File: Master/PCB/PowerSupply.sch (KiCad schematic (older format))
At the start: 32 parts, among them J20 Jumper, Q28 BSS138, Q29 BSS138, Q30 BSS138, U19 LM5165YDRC

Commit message: Update
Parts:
- C89, C90: value 1u -> 10u; footprint Capacitors_SMD:C_0603_HandSoldering -> Capacitor_SMD:C_0805_2012Metric
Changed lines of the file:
@@
 $Descr A2 23386 16535
 encoding utf-8
-Sheet 8 8
+Sheet 7 8
 Title ""
 Date ""
@@
 P 12400 6850
 F 0 "C90" H 12200 6800 50  0000 L CNN
-F 1 "1u" H 12200 6900 50  0000 L CNN
-F 2 "Capacitors_SMD:C_0603_HandSoldering" H 12438 6700 50  0001 C CNN
+F 1 "10u" H 12200 6900 50  0000 L CNN
+F 2 "Capacitor_SMD:C_0805_2012Metric" H 12438 6700 50  0001 C CNN
 F 3 "~" H 12400 6850 50  0001 C CNN
 F 4 "50V" H 12400 6850 50  0001 C CNN "Volatge"
@@
 P 11900 6850
 F 0 "C89" H 11700 6800 50  0000 L CNN
-F 1 "1u" H 11700 6900 50  0000 L CNN
-F 2 "Capacitors_SMD:C_0603_HandSoldering" H 11938 6700 50  0001 C CNN
+F 1 "10u" H 11700 6900 50  0000 L CNN
+F 2 "Capacitor_SMD:C_0805_2012Metric" H 11938 6700 50  0001 C CNN
 F 3 "~" H 11900 6850 50  0001 C CNN
 F 4 "50V" H 11900 6850 50  0001 C CNN "Volatge"

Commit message: Current sensors updates & master
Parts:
- C89, C90: footprint Capacitor_SMD:C_0805_2012Metric -> Capacitors_SMD:C_0805_HandSoldering
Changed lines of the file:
@@
 EESchema Schematic File Version 5
 LIBS:BMS-Master-cache
-EELAYER 29 0
+EELAYER 30 0
 EELAYER END
 $Descr A2 23386 16535
 encoding utf-8
-Sheet 7 8
+Sheet 6 7
 Title ""
 Date ""
@@
 F 0 "C90" H 12200 6800 50  0000 L CNN
 F 1 "10u" H 12200 6900 50  0000 L CNN
-F 2 "Capacitor_SMD:C_0805_2012Metric" H 12438 6700 50  0001 C CNN
+F 2 "Capacitors_SMD:C_0805_HandSoldering" H 12438 6700 50  0001 C CNN
 F 3 "~" H 12400 6850 50  0001 C CNN
 F 4 "50V" H 12400 6850 50  0001 C CNN "Volatge"
@@
 F 0 "C89" H 11700 6800 50  0000 L CNN
 F 1 "10u" H 11700 6900 50  0000 L CNN
-F 2 "Capacitor_SMD:C_0805_2012Metric" H 11938 6700 50  0001 C CNN
+F 2 "Capacitors_SMD:C_0805_HandSoldering" H 11938 6700 50  0001 C CNN
 F 3 "~" H 11900 6850 50  0001 C CNN
 F 4 "50V" H 11900 6850 50  0001 C CNN "Volatge"

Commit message: BOM
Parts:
- C88, C89, C90, C91, C92, C93, C94: symbol BMS-Master-rescue:C-Device -> BMS-Master-rescue:C-Device-BMS-Master-rescue
- J20: symbol BMS-Master-rescue:Conn_01x01-Connector_Generic -> BMS-Master-rescue:Conn_01x01-Connector_Generic-BMS-Master-rescue
- R172, R173, R174, R175, R176, R177, R178, R179, R180, R181, R182, R183: symbol BMS-Master-rescue:R-Device -> BMS-Master-rescue:R-Device-BMS-Master-rescue
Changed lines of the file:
@@
 EESchema Schematic File Version 5
 LIBS:BMS-Master-cache
-EELAYER 30 0
+EELAYER 29 0
 EELAYER END
 $Descr A2 23386 16535
@@
 $EndComp
 $Comp
-L BMS-Master-rescue:C-Device C90
+L BMS-Master-rescue:C-Device-BMS-Master-rescue C90
 U 1 1 5C6103A5
 P 12400 6850
@@
 $EndComp
 $Comp
-L BMS-Master-rescue:C-Device C89
+L BMS-Master-rescue:C-Device-BMS-Master-rescue C89
 U 1 1 5C61074A
 P 11900 6850
@@
 	12400 6700 12400 6400
 $Comp
-L BMS-Master-rescue:GND-power #PWR0251
+L BMS-Master-rescue:GND-power-BMS-Master-rescue #PWR0251
 U 1 1 5C6188F7
 P 11900 7350
@@
 	11900 7000 11900 7350
 $Comp
-L BMS-Master-rescue:GND-power #PWR0252
+L BMS-Master-rescue:GND-power-BMS-Master-rescue #PWR0252
 U 1 1 5C61B805
 P 12400 7350
@@
 Connection ~ 13350 7150
 $Comp
-L BMS-Master-rescue:GND-power #PWR0253
+L BMS-Master-rescue:GND-power-BMS-Master-rescue #PWR0253
 U 1 1 5C69C12E
 P 13900 7600
@@
 	13900 7350 13900 7600
 $Comp
-L BMS-Master-rescue:R-Device R179
+L BMS-Master-rescue:R-Device-BMS-Master-rescue R179
 U 1 1 5C69FE87
 P 14400 7250
@@
 	14400 7000 14500 7000
 $Comp
-L BMS-Master-rescue:R-Device R177
+L BMS-Master-rescue:R-Device-BMS-Master-rescue R177
 U 1 1 5C627140
 P 13750 6800
@@
 $EndComp
 $Comp
-L BMS-Master-rescue:R-Device R175
+L BMS-Master-rescue:R-Device-BMS-Master-rescue R175
 U 1 1 5C623C3B
 P 13350 6800
@@
 $EndComp
 $Comp
-L BMS-Master-rescue:GND-power #PWR0254
+L BMS-Master-rescue:GND-power-BMS-Master-rescue #PWR0254
 U 1 1 5C6A8028
 P 13350 7600
@@
 	13700 8500 14650 8500
 $Comp
-L BMS-Master-rescue:R-Device R178
+L BMS-Master-rescue:R-Device-BMS-Master-rescue R178
 U 1 1 5C6F3B76
 P 14150 9100
@@
 	15850 6600 15850 6400
 $Comp
-L BMS-Master-rescue:GND-power #PWR0255
+L BMS-Master-rescue:GND-power-BMS-Master-rescue #PWR0255
 U 1 1 5C713381
 P 14400 7600
@@
 	13400 10700 13650 10700
 $Comp
-L BMS-Master-rescue:R-Device R176
+L BMS-Master-rescue:R-Device-BMS-Master-rescue R176
 U 1 1 5C72D283
 P 13650 10850
@@
 	13650 10700 13850 10700
 $Comp
-L BMS-Master-rescue:GND-power #PWR0256
+L BMS-Master-rescue:GND-power-BMS-Master-rescue #PWR0256
 U 1 1 5C72DA2B
 P 13650 11100
@@
 Connection ~ 13650 11100
 $Comp
-L BMS-Master-rescue:R-Device R182
+L BMS-Master-rescue:R-Device-BMS-Master-rescue R182
 U 1 1 5C737745
 P 16900 6400
@@
 Connection ~ 15850 6400
 $Comp
-L BMS-Master-rescue:R-Device R180
+L BMS-Master-rescue:R-Device-BMS-Master-rescue R180
 U 1 1 5C7417D6
 P 16250 6850
@@
 $EndComp
 $Comp
-L BMS-Master-rescue:GND-power #PWR0257
+L BMS-Master-rescue:GND-power-BMS-Master-rescue #PWR0257
 U 1 1 5C7421FF
 P 16250 7700
@@
 $EndComp
 $Comp
-L BMS-Master-rescue:C-Device C92
+L BMS-Master-rescue:C-Device-BMS-Master-rescue C92
 U 1 1 5C742B3F
 P 16250 7350
@@
 	16550 7500 16550 7700
 $Comp
-L BMS-Master-rescue:C-Device C93
+L BMS-Master-rescue:C-Device-BMS-Master-rescue C93
 U 1 1 5C742FAA
 P 16550 7350
@@
 $EndComp
 $Comp
-L BMS-Master-rescue:GND-power #PWR0258
+L BMS-Master-rescue:GND-power-BMS-Master-rescue #PWR0258
 U 1 1 5C74287E
 P 16550 7700
@@
 $EndComp
 $Comp
-L BMS-Master-rescue:R-Device R181
+L BMS-Master-rescue:R-Device-BMS-Master-rescue R181
 U 1 1 5C741EBD
 P 16550 6850
@@
 	17450 7500 17450 7700
 $Comp
-L BMS-Master-rescue:C-Device C94
+L BMS-Master-rescue:C-Device-BMS-Master-rescue C94
 U 1 1 5C773AC8
 P 17450 7350
@@
 $EndComp
 $Comp
-L BMS-Master-rescue:GND-power #PWR0259
+L BMS-Master-rescue:GND-power-BMS-Master-rescue #PWR0259
 U 1 1 5C773ACE
 P 17450 7700
@@
 $EndComp
 $Comp
-L BMS-Master-rescue:R-Device R183
+L BMS-Master-rescue:R-Device-BMS-Master-rescue R183
 U 1 1 5C773AD4
 P 17450 6850
@@
 	14900 7200 14800 7200
 $Comp
-L BMS-Master-rescue:GND-power #PWR0260
+L BMS-Master-rescue:GND-power-BMS-Master-rescue #PWR0260
 U 1 1 5C783ED4
 P 14900 7650
@@
 	14900 7200 14900 7650
 $Comp
-L BMS-Master-rescue:C-Device C91
+L BMS-Master-rescue:C-Device-BMS-Master-rescue C91
 U 1 1 5C789CBC
 P 15600 7300
@@
 $EndComp
 $Comp
-L BMS-Master-rescue:GND-power #PWR0261
+L BMS-Master-rescue:GND-power-BMS-Master-rescue #PWR0261
 U 1 1 5C78A045
 P 15600 7700
@@
 	13350 9100 13450 9100
 $Comp
-L BMS-Master-rescue:R-Device R174
+L BMS-Master-rescue:R-Device-BMS-Master-rescue R174
 U 1 1 5C7ABCF5
 P 11550 10150
@@
 $EndComp
 $Comp
-L BMS-Master-rescue:C-Device C88
+L BMS-Master-rescue:C-Device-BMS-Master-rescue C88
 U 1 1 5C7AC205
 P 11550 9800
@@
 	9950 10400 10900 10400
 $Comp
-L BMS-Master-rescue:GND-power #PWR0264
+L BMS-Master-rescue:GND-power-BMS-Master-rescue #PWR0264
 U 1 1 5C7F2939
 P 10900 10800
@@
 	10900 10700 10900 10800
 $Comp
-L BMS-Master-rescue:GND-power #PWR0265
+L BMS-Master-rescue:GND-power-BMS-Master-rescue #PWR0265
 U 1 1 5C7FA642
 P 9650 10800
@@
 	9650 10600 9650 10800
 $Comp
-L BMS-Master-rescue:R-Device R172
+L BMS-Master-rescue:R-Device-BMS-Master-rescue R172
 U 1 1 5C8028F6
 P 9900 9800
@@
 	11400 9150 11650 9150
 $Comp
-L BMS-Master-rescue:R-Device R173
+L BMS-Master-rescue:R-Device-BMS-Master-rescue R173
 U 1 1 5C8228C0
 P 10800 9150
@@
 Connection ~ 8650 5800
 $Comp
-L BMS-Master-rescue:Conn_01x01-Connector_Generic J20
+L BMS-Master-rescue:Conn_01x01-Connector_Generic-BMS-Master-rescue J20
 U 1 1 5C86E7FA
 P 8650 5600

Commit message: Nothing
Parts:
- removed J20: Jumper, TestPoint:TestPoint_Loop_D2.54mm_Drill1.5mm_Beaded, symbol BMS-Master-rescue:Conn_01x01-Connector_Generic-BMS-Master-rescue
- R175, R177: footprint Resistors_SMD:R_0805_HandSoldering -> Resistors_SMD:R_0603_HandSoldering
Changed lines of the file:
@@
 $Descr A2 23386 16535
 encoding utf-8
-Sheet 5 7
+Sheet 4 7
 Title ""
 Date ""
@@
 Comment3 ""
 Comment4 ""
-Comment5 ""
-Comment6 ""
-Comment7 ""
-Comment8 ""
-Comment9 ""
 $EndDescr
 Text HLabel 9400 9800 0    50   Input ~ 0
@@
 F 0 "R177" H 13680 6754 50  0000 R CNN
 F 1 "4.7M" H 13680 6845 50  0000 R CNN
-F 2 "Resistors_SMD:R_0805_HandSoldering" V 13680 6800 50  0001 C CNN
+F 2 "Resistors_SMD:R_0603_HandSoldering" V 13680 6800 50  0001 C CNN
 F 3 "~" H 13750 6800 50  0001 C CNN
 	1    13750 6800
@@
 F 0 "R175" H 13280 6754 50  0000 R CNN
 F 1 "4.7M" H 13280 6845 50  0000 R CNN
-F 2 "Resistors_SMD:R_0805_HandSoldering" V 13280 6800 50  0001 C CNN
+F 2 "Resistors_SMD:R_0603_HandSoldering" V 13280 6800 50  0001 C CNN
 F 3 "~" H 13350 6800 50  0001 C CNN
 	1    13350 6800
@@
 Wire Wire Line
 	8650 5800 8650 6400
-Connection ~ 8650 5800
-$Comp
-L BMS-Master-rescue:Conn_01x01-Connector_Generic-BMS-Master-rescue J20
-U 1 1 5C86E7FA
-P 8650 5600
-F 0 "J20" V 8614 5512 50  0000 R CNN
-F 1 "Jumper" V 8523 5512 50  0000 R CNN
-F 2 "TestPoint:TestPoint_Loop_D2.54mm_Drill1.5mm_Beaded" H 8650 5600 50  0001 C CNN
-F 3 "" H 8650 5600 50  0001 C CNN
-	1    8650 5600
-	0    -1   -1   0
-$EndComp
 Wire Wire Line
 	8650 6400 11900 6400

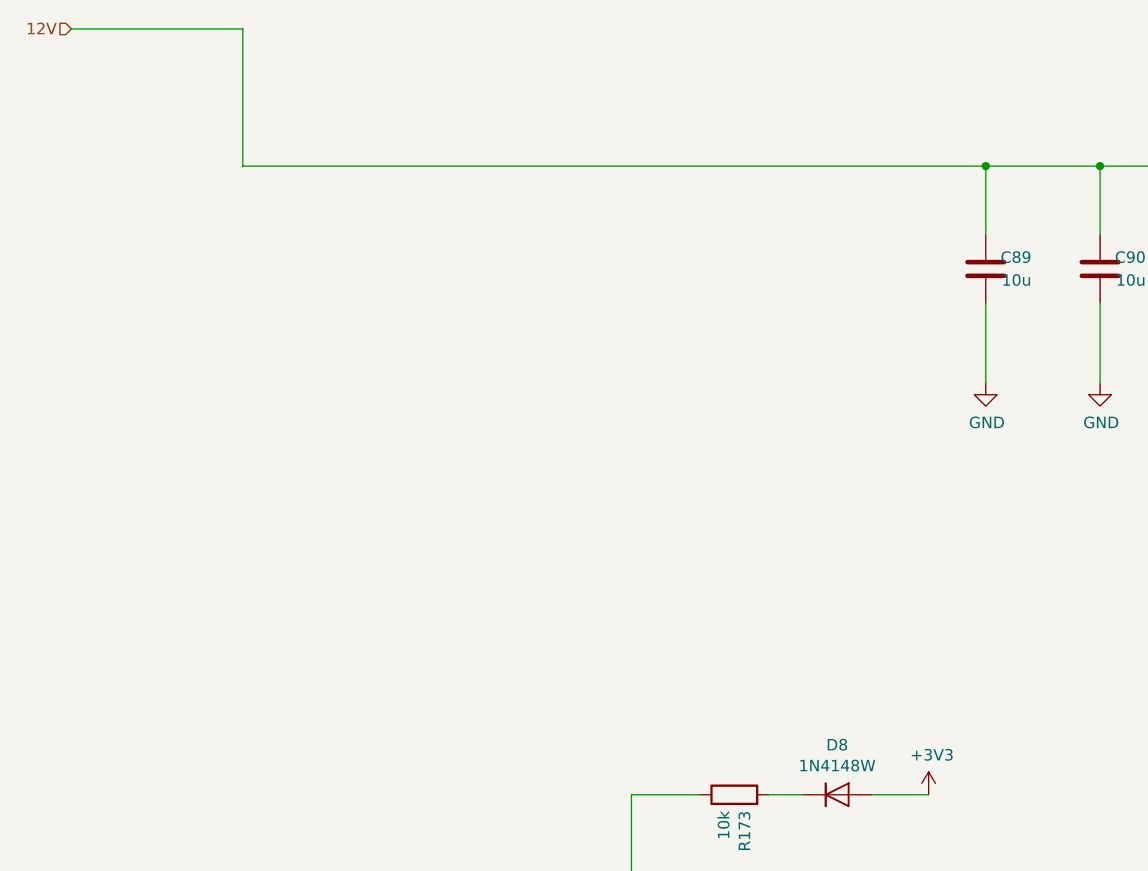
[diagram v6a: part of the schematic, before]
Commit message: Added charger detect from 12V charger Aux
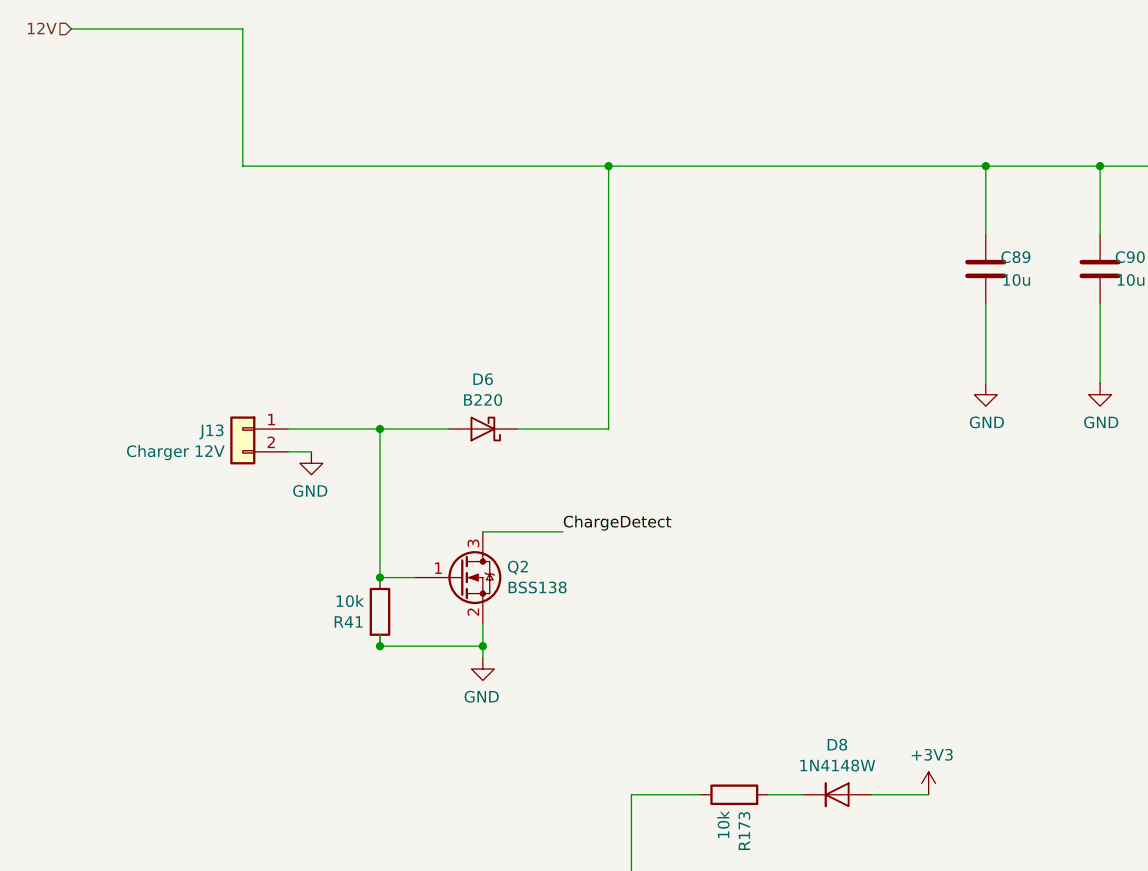
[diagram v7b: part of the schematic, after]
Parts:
- added D6: B220, Diode_SMD:D_SMB, symbol Diode:B220
- added J13: Charger 12V, Connectors_Molex:Molex_KK-6410-02_02x2.54mm_Straight, symbol BMS-Master-rescue:Conn_01x02-Connector_Generic-BMS-Master-rescue
- added Q2: BSS138, TO_SOT_Packages_SMD:SOT-23, symbol Transistor_FET:BSS138
- added R41: 10k, Resistors_SMD:R_0603_HandSoldering, symbol BMS-Master-rescue:R-Device-BMS-Master-rescue
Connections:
- net 12V: now also D6.1 (K)
- net ChargeDetect: now also Q2.3 (D)
- net GND: now also J13.2 (Pin_2), Q2.2 (S), R41.2
- new net: D6.2 (A), J13.1 (Pin_1), Q2.1 (G), R41.1
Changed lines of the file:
@@
 Text HLabel 14650 8500 2    50   Input ~ 0
 EnableFromExt
-Text HLabel 14600 9800 2    50   Input ~ 0
-ChargeDetect
 Wire Wire Line
 	13350 7150 13100 7150
@@
 Wire Wire Line
 	13700 8500 14650 8500
-$Comp
-L BMS-Master-rescue:R-Device-BMS-Master-rescue R178
-U 1 1 5C6F3B76
-P 14150 9100
-F 0 "R178" H 14080 9054 50  0000 R CNN
-F 1 "10k" H 14080 9145 50  0000 R CNN
-F 2 "Resistors_SMD:R_0603_HandSoldering" V 14080 9100 50  0001 C CNN
-F 3 "~" H 14150 9100 50  0001 C CNN
-	1    14150 9100
-	0    -1   -1   0
-$EndComp
-Wire Wire Line
-	13750 9800 14600 9800
-Wire Wire Line
-	14600 9800 14600 9100
 Wire Wire Line
 	14600 9100 14300 9100
@@
 	8650 5800 8650 6400
 Wire Wire Line
-	8650 6400 11900 6400
+	8650 6400 10250 6400
+$Comp
+L BMS-Master-rescue:Conn_01x02-Connector_Generic-BMS-Master-rescue J13
+U 1 1 5D833BBD
+P 8650 7550
+F 0 "J13" H 8729 7542 50  0000 L CNN
+F 1 "Charger 12V" H 8729 7451 50  0000 L CNN
+F 2 "Connectors_Molex:Molex_KK-6410-02_02x2.54mm_Straight" H 8650 7550 50  0001 C CNN
+F 3 "~" H 8650 7550 50  0001 C CNN
+	1    8650 7550
+	-1   0    0    -1
+$EndComp
+$Comp
+L BMS-Master-rescue:GND-power-BMS-Master-rescue #PWR0147
+U 1 1 5D833BBE
+P 8950 7650
+F 0 "#PWR0147" H 8950 7400 50  0001 C CNN
+F 1 "GND" H 8955 7477 50  0000 C CNN
+F 2 "" H 8950 7650 50  0001 C CNN
+F 3 "" H 8950 7650 50  0001 C CNN
+	1    8950 7650
+	-1   0    0    -1
+$EndComp
+Wire Wire Line
+	8850 7650 8950 7650
+Wire Wire Line
+	10250 7550 10250 6400
+Connection ~ 10250 6400
+Wire Wire Line
+	10250 6400 11900 6400
+$Comp
+L BMS-Master-rescue:R-Device-BMS-Master-rescue R178
+U 1 1 5C6F3B76
+P 14150 9100
+F 0 "R178" H 14080 9054 50  0000 R CNN
+F 1 "10k" H 14080 9145 50  0000 R CNN
+F 2 "Resistors_SMD:R_0603_HandSoldering" V 14080 9100 50  0001 C CNN
+F 3 "~" H 14150 9100 50  0001 C CNN
+	1    14150 9100
+	0    -1   -1   0
+$EndComp
+Text HLabel 14600 9800 2    50   Input ~ 0
+ChargeDetect
+Wire Wire Line
+	14600 9800 14600 9100
+Wire Wire Line
+	13750 9800 14600 9800
+Wire Wire Line
+	9850 7550 10250 7550
+$Comp
+L Diode:B220 D6
+U 1 1 5D83524C
+P 9700 7550
+F 0 "D6" H 9700 7334 50  0000 C CNN
+F 1 "B220" H 9700 7425 50  0000 C CNN
+F 2 "Diode_SMD:D_SMB" H 9700 7375 50  0001 C CNN
+F 3 "http://www.jameco.com/Jameco/Products/ProdDS/1538777.pdf" H 9700 7550 50  0001 C CNN
+	1    9700 7550
+	-1   0    0    1
+$EndComp
+Wire Wire Line
+	8850 7550 9250 7550
+$Comp
+L Transistor_FET:BSS138 Q2
+U 1 1 5D859451
+P 9600 8200
+F 0 "Q2" H 9806 8246 50  0000 L CNN
+F 1 "BSS138" H 9806 8155 50  0000 L CNN
+F 2 "TO_SOT_Packages_SMD:SOT-23" H 9800 8125 50  0001 L CIN
+F 3 "https://www.fairchildsemi.com/datasheets/BS/BSS138.pdf" H 9600 8200 50  0001 L CNN
+	1    9600 8200
+	1    0    0    -1
+$EndComp
+$Comp
+L BMS-Master-rescue:GND-power-BMS-Master-rescue #PWR0148
+U 1 1 5D861B52
+P 9700 8550
+F 0 "#PWR0148" H 9700 8300 50  0001 C CNN
+F 1 "GND" H 9705 8377 50  0000 C CNN
+F 2 "" H 9700 8550 50  0001 C CNN
+F 3 "" H 9700 8550 50  0001 C CNN
+	1    9700 8550
+	-1   0    0    -1
+$EndComp
+Wire Wire Line
+	9700 8400 9700 8500
+Wire Wire Line
+	9250 7550 9250 8200
+Wire Wire Line
+	9250 8200 9400 8200
+Connection ~ 9250 7550
+Wire Wire Line
+	9250 7550 9550 7550
+$Comp
+L BMS-Master-rescue:R-Device-BMS-Master-rescue R41
+U 1 1 5D862412
+P 9250 8350
+F 0 "R41" H 9180 8304 50  0000 R CNN
+F 1 "10k" H 9180 8395 50  0000 R CNN
+F 2 "Resistors_SMD:R_0603_HandSoldering" V 9180 8350 50  0001 C CNN
+F 3 "~" H 9250 8350 50  0001 C CNN
+	1    9250 8350
+	1    0    0    -1
+$EndComp
+Connection ~ 9250 8200
+Wire Wire Line
+	9250 8450 9250 8500
+Wire Wire Line
+	9250 8500 9700 8500
+Connection ~ 9250 8500
+Connection ~ 9700 8500
+Wire Wire Line
+	9700 8500 9700 8550
+Text Label 10050 8000 0    50   ~ 0
+ChargeDetect
+Wire Wire Line
+	9700 8000 10050 8000
 $EndSCHEMATC
